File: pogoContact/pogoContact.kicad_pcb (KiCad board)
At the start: 2 copper layers, 36.9 x 41 mm, 6 parts, among them J1 Conn_01x06, J2 Conn_01x03, J3 Conn_01x03

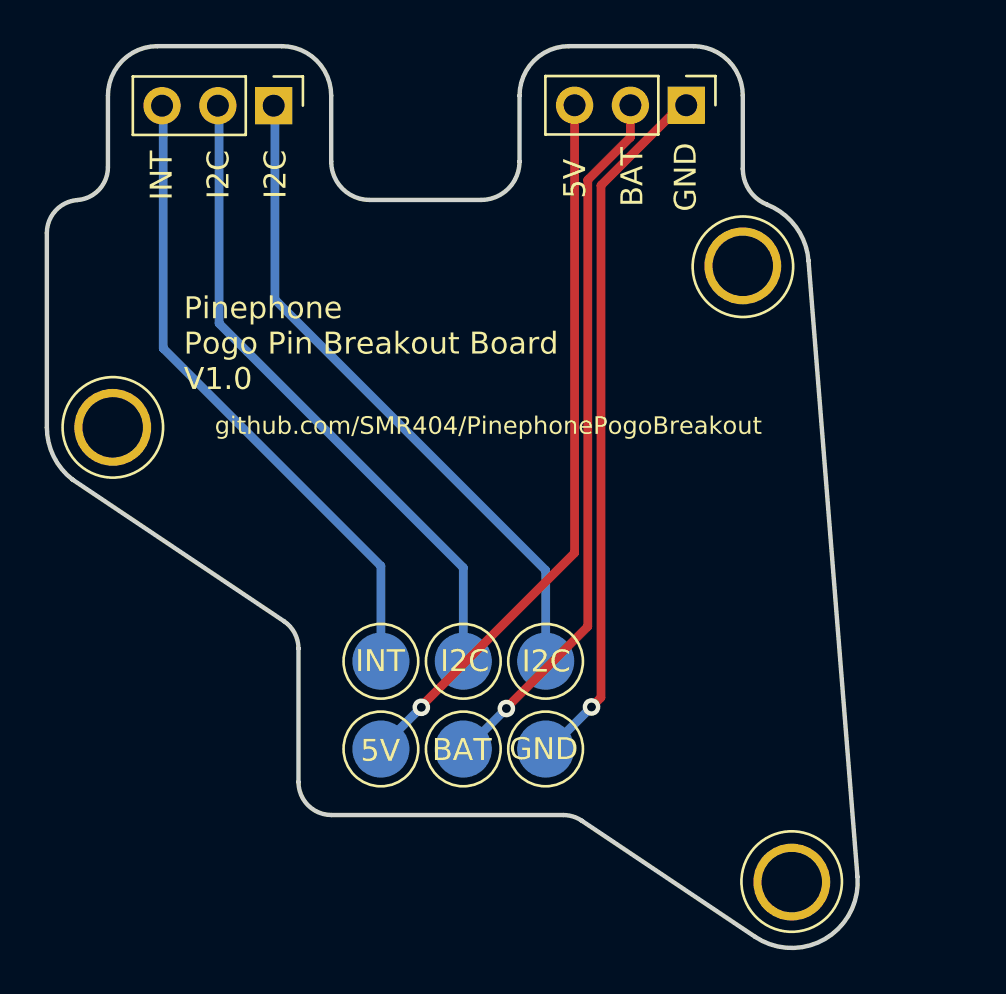
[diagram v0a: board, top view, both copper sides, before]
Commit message: Add files via upload
simplyfied the board to a single side design and easier to cut.
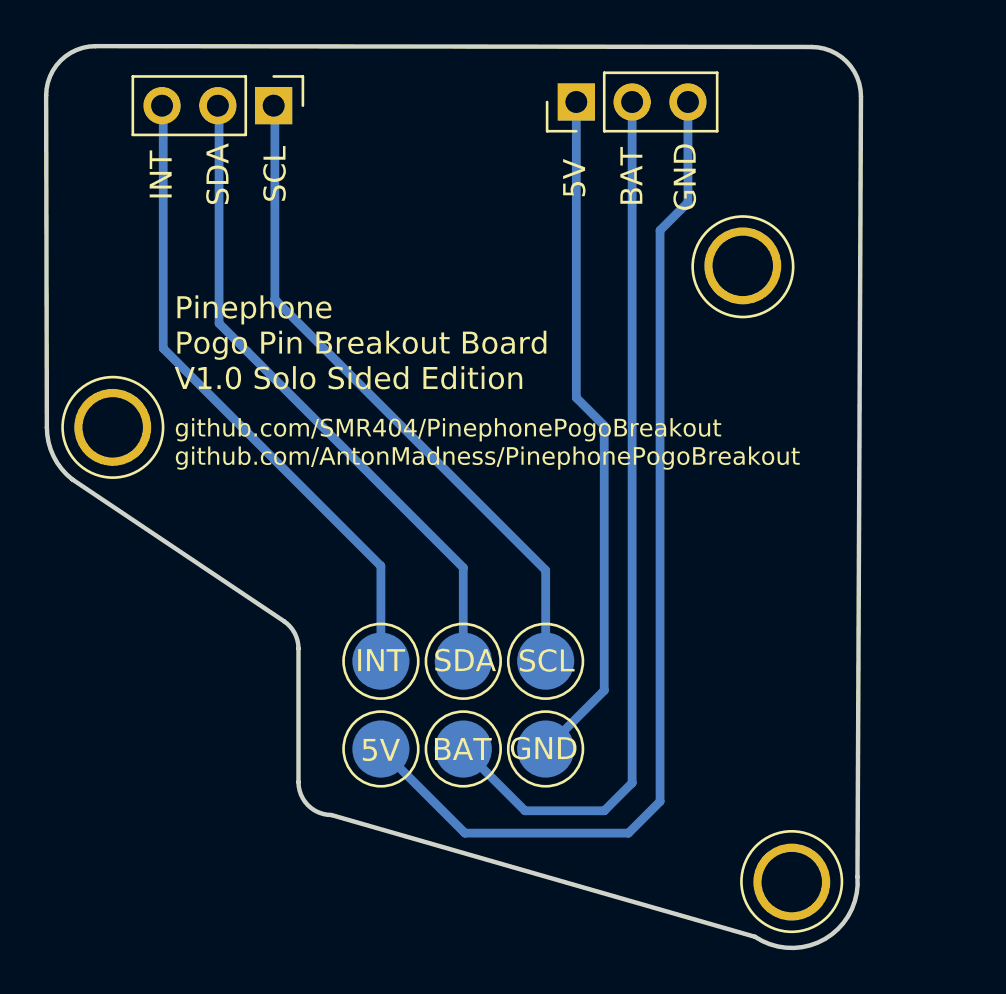
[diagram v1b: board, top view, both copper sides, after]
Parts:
- moved J3 5.00 mm to (149.9, 57.9), turned to 90 degrees
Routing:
- net Net-(J1-Pad6): track 33.3 -> 47.6 mm, vias 1 -> 0
- net Net-(J1-Pad5): track 32.7 -> 40.7 mm, vias 1 -> 0
- net Net-(J1-Pad4): track 32.2 -> 31.2 mm, vias 1 -> 0
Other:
- board size 36.9 x 41 mm -> 37.1 x 41 mm
- board text added: "Pinephone Pogo Pin Breakout Board V1.0 Solo Sided Edition"
- board text added: "SCL"
- board text added: "SDA"
- board text added: "github.com/SMR404/PinephonePogoBreakout github.com/AntonMadness/PinephonePogoBreakout"
- board text removed: "I2C"
- board text removed: "Pinephone Pogo Pin Breakout Board V1.0"
- board text removed: "github.com/SMR404/PinephonePogoBreakout"
